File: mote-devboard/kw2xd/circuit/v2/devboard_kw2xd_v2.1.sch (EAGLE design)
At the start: 21 parts, among them J1 CORTEX_DEBUG_PTH, Q1 RED, Q2 RED, Q3 GREEN

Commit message: WIP
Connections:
- removed net PTA1: PORT_A.2
- net PTA1_TDI: now also PORT_A.2
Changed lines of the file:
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@@
-</segment>
-</net>
-<net name="PTA1" class="0">
-<segment>
-<pinref part="PORT_A" gate="G$1" pin="2"/>
-<wire x1="198.12" y1="149.86" x2="182.88" y2="149.86" width="0.1524" layer="91"/>
-<label x="180.34" y="149.86" size="1.778" layer="95"/>
 </segment>
 </net>
@@
 <label x="248.92" y="50.8" size="1.778" layer="95"/>
 </segment>
+<segment>
+<pinref part="PORT_A" gate="G$1" pin="2"/>
+<wire x1="198.12" y1="149.86" x2="182.88" y2="149.86" width="0.1524" layer="91"/>
+<label x="180.34" y="149.86" size="1.778" layer="95"/>
+</segment>
 </net>

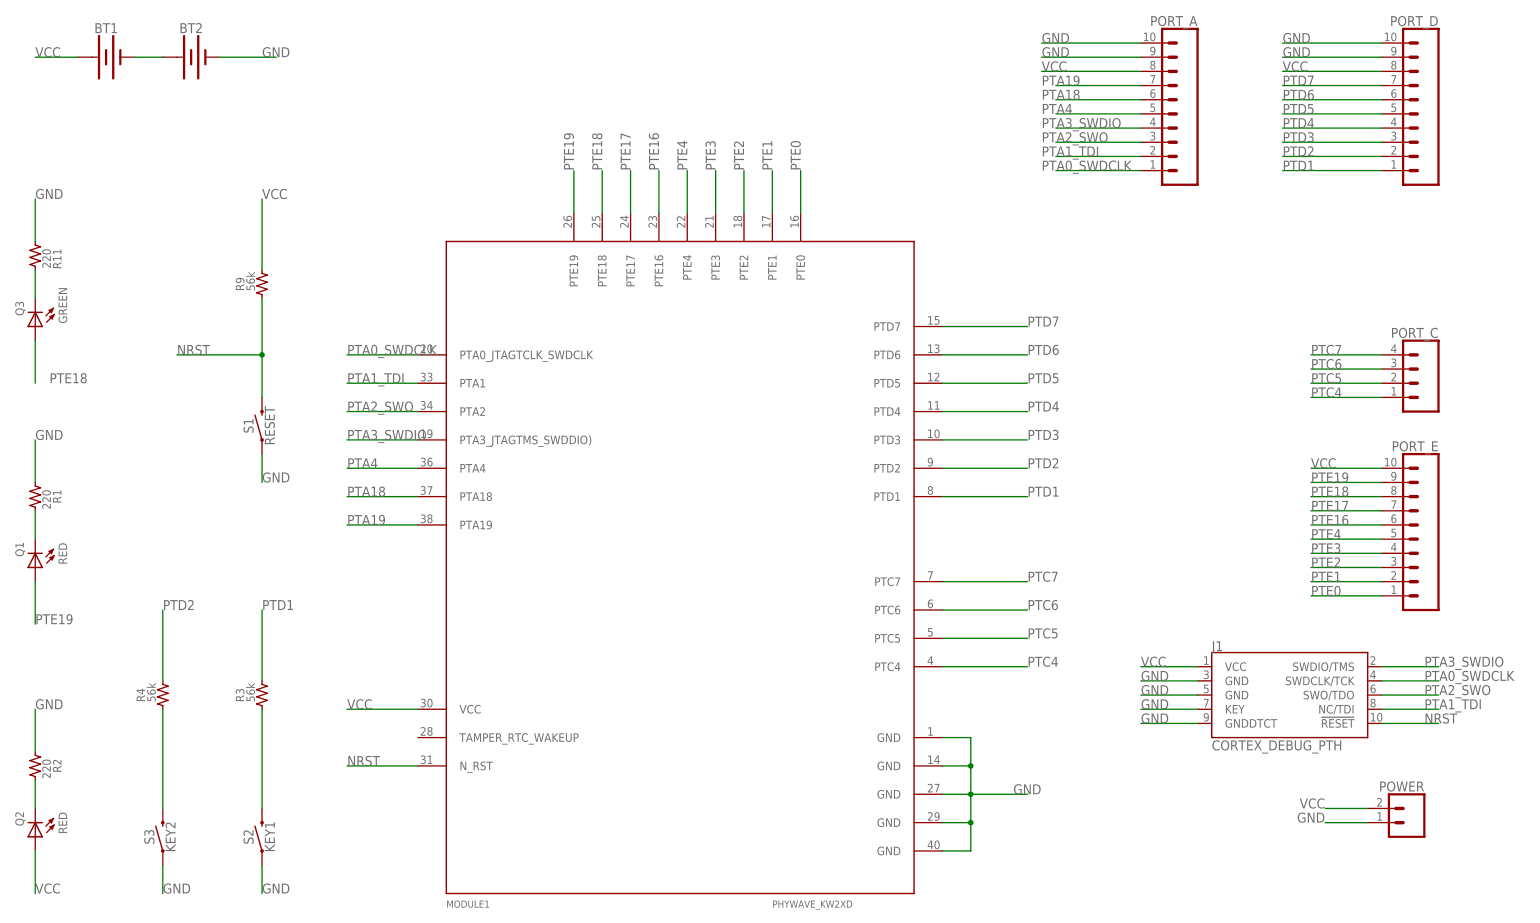
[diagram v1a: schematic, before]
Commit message: 2-pin header (upper left) will be used as power switch/current meter
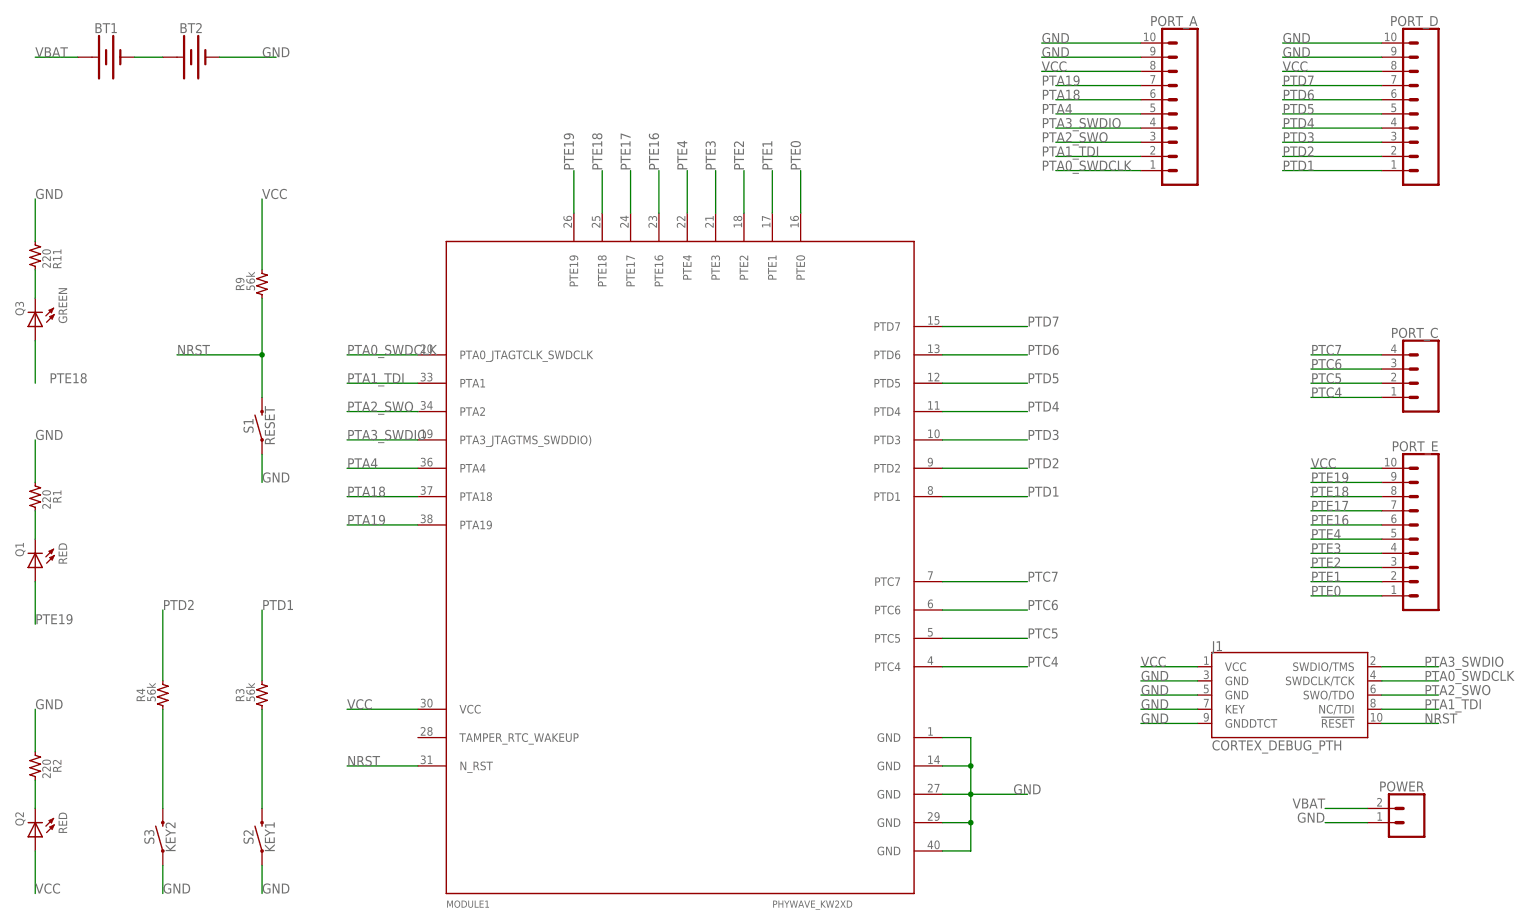
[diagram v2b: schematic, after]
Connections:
- new net VBAT: BT1.+, POWER.2
- net VCC: no longer BT1.+, POWER.2
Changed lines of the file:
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@@
-</segment>
-<segment>
-<pinref part="POWER" gate="G$1" pin="2"/>
-<wire x1="238.76" y1="33.02" x2="231.14" y2="33.02" width="0.1524" layer="91"/>
-<label x="231.14" y="33.02" size="1.778" layer="95" rot="MR0"/>
 </segment>
 <segment>
@@
 <wire x1="208.28" y1="58.42" x2="198.12" y2="58.42" width="0.1524" layer="91"/>
 <label x="198.12" y="58.42" size="1.778" layer="95"/>
-</segment>
-<segment>
-<pinref part="BT1" gate="G$1" pin="+"/>
-<wire x1="7.62" y1="167.64" x2="0" y2="167.64" width="0.1524" layer="91"/>
-<label x="0" y="167.64" size="1.778" layer="95"/>
 </segment>
 </net>
@@
 </segment>
 </net>
+<net name="VBAT" class="0">
+<segment>
+<pinref part="BT1" gate="G$1" pin="+"/>
+<wire x1="7.62" y1="167.64" x2="0" y2="167.64" width="0.1524" layer="91"/>
+<label x="0" y="167.64" size="1.778" layer="95"/>
+</segment>
+<segment>
+<pinref part="POWER" gate="G$1" pin="2"/>
+<wire x1="238.76" y1="33.02" x2="231.14" y2="33.02" width="0.1524" layer="91"/>
+<label x="231.14" y="33.02" size="1.778" layer="95" rot="MR0"/>
+</segment>
+</net>

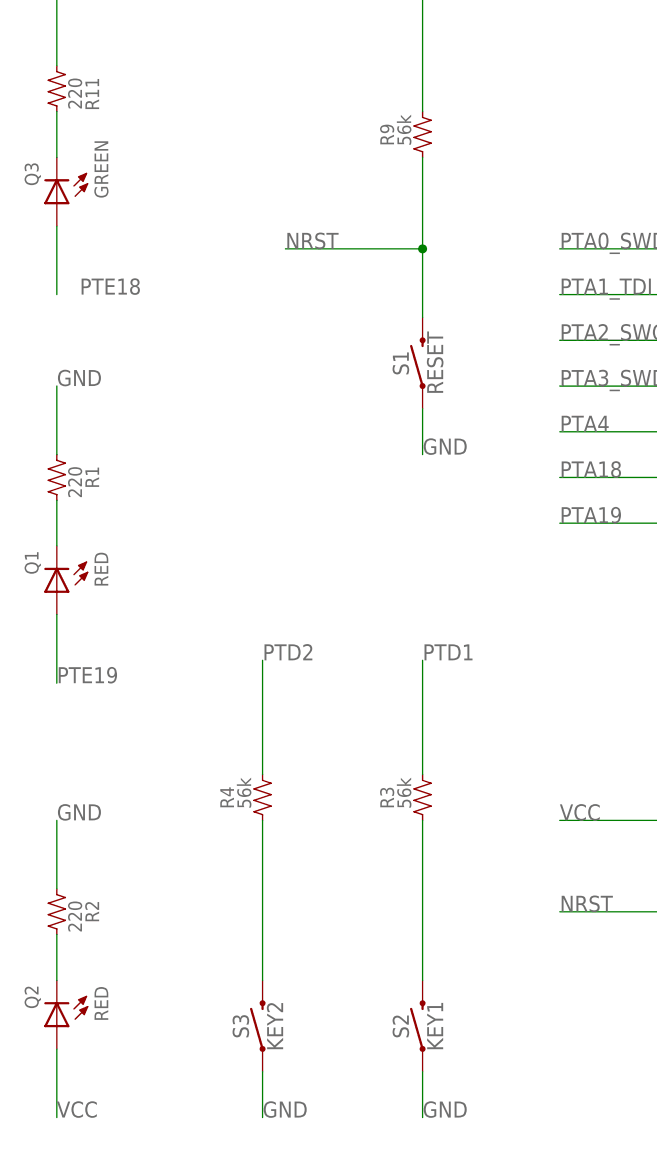
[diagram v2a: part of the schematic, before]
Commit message: Changed cpu mode to FEI so we don't rely on radio clock Minor changes in board design
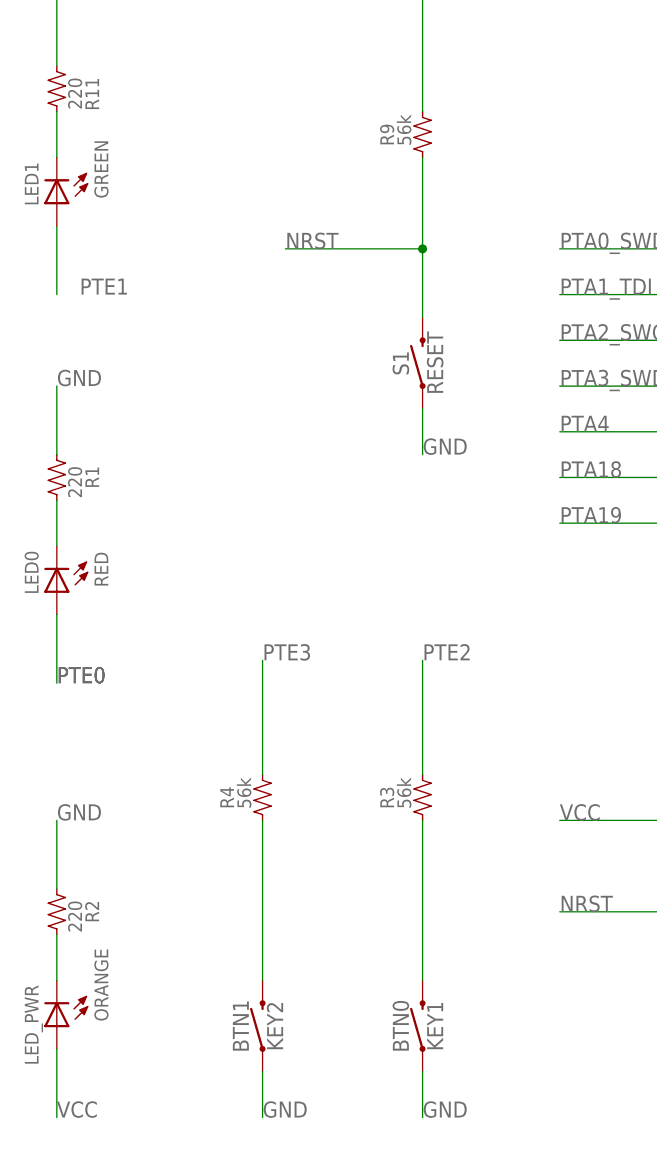
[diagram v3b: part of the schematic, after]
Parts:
- LED_PWR: value RED -> ORANGE
- renumbered Q1 to LED0, Q2 to LED_PWR, Q3 to LED1, S2 to BTN0, S3 to BTN1
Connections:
- net PTD1: no longer R3.2
- net PTD2: no longer R4.2
- net PTE0: now also LED0.A
- net PTE1: now also LED1.A
- net PTE18: no longer LED1.A
- net PTE19: no longer LED0.A
- net PTE2: now also R3.2
- net PTE3: now also R4.2
